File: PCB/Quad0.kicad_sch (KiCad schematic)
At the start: 0 parts

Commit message: implemented basic rp2350 devboard schematics
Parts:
- added C1, C2: 10uF, symbol Device:C_Small
- added C10, C11, C12, C13, C14, C15, C16, C17, C7, C8, C9: 0.1uF, symbol Device:C_Small
- added C18, C19: 15pF, symbol Device:C_Small
- added C3, C4, C5: 4.7uF, symbol Device:C_Small
- added C6: 10u, symbol Device:C_Small
- added J1: DEBUG_CONN_PAD, symbol Connector_Generic:Conn_01x05
- added L1: 3.3u, symbol Device:L_Small
- added Q1: Si2302CDS-T1-GE3, easyeda2kicad:SOT-23_L2.9-W1.3-P1.90-LS2.4-BR, symbol easyeda2kicad:Si2302CDS-T1-GE3
- added R1, R2: 5.1k, symbol Device:R_Small
- added R10, R6, R8, R9: 1k, symbol Device:R_Small
- added R3: 33, symbol Device:R_Small
- added R4, R5: 27, symbol Device:R_Small
- added R7: 10k, symbol Device:R_Small
- added SW1: RUN_BTN, easyeda2kicad:SW-SMD_L3.9-W3.0-P4.45, symbol easyeda2kicad:TS-1088-AR02016
- added SW2: BOOTSEL_BTN, easyeda2kicad:SW-SMD_L3.9-W3.0-P4.45, symbol easyeda2kicad:TS-1088-AR02016
- added U1: RP2350A_C42411118, easyeda2kicad:QFN-60_L7.0-W7.0-P0.40-TL-EP3.4, symbol easyeda2kicad:RP2350A_C42411118
- added U2: AP7361C-33E-13, easyeda2kicad:SOT-223_L6.5-W3.5-P2.30-LS7.0-BR, symbol easyeda2kicad:AP7361C-33E-13
- added U3: W25Q128JVSIQTR, easyeda2kicad:SOIC-8_L5.3-W5.3-P1.27-LS8.0-BL, symbol easyeda2kicad:W25Q128JVSIQTR
- added U4: ABM8-272-T3_C20625731, easyeda2kicad:CRYSTAL-SMD_4P-L3.2-W2.5-BL, symbol easyeda2kicad:ABM8-272-T3_C20625731
- added USB1: TYPE-C 16PIN 2MD, easyeda2kicad:USB-C-SMD_TYPE-C-16PIN-2MD-073, symbol easyeda2kicad:TYPE-C16PIN2MD
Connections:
- new net: R8.1, SW2.2
- new net: C19.2, R10.2, U4.3
- new net: R5.2, U1.51 (USB_DM)
- new net: R6.1, SW1.2
- new net: R2.1, USB1.A5 (CC1)
- new net: R1.1, USB1.B5 (CC2)
- new net: R4.1, U1.52 (USB_DP)
- new net: C3.1, R3.2, U1.46 (VREG_AVDD)
- new net: L1.2, U1.48 (VREG_LX)
- new net +1V1: C15.2, C16.2, C17.2, C5.2, L1.1, U1.23 (DVDD), U1.39 (DVDD), U1.50 (VREG_FB), U1.6 (DVDD)
- new net +3.3V: C10.2, C11.2, C12.2, C13.2, C14.2, C2.1, C4.2, C6.1, C7.1, C8.2, C9.2, R3.1, R7.1, U1.1 (IOVDD), U1.11 (IOVDD), U1.20 (IOVDD), U1.30 (IOVDD), U1.38 (IOVDD), U1.44 (ADC_AVDD), U1.45 (IOVDD), U1.49 (VREG_VIN), U1.53 (USB_OTP_VDD), U1.54 (QSPI_IOVDD), U2.3 (OUT), U3.8 (VCC)
- new net GND: C1.2, C10.1, C11.1, C12.1, C13.1, C14.1, C15.1, C16.1, C17.1, C18.1, C19.1, C2.2, C3.2, C4.1, C5.1, C6.2, C7.2, C8.1, C9.1, J1.1 (Pin_1), J1.2 (Pin_2), J1.4 (Pin_4), R1.2, R2.2, R6.2, R8.2, U1.47 (VREG_PGND), U1.61 (GND), U2.2 (GND), U2.4 (GND), U3.4 (GND), U4.2 (GND), U4.4 (GND), USB1.13 (EH), USB1.14 (EH), USB1.A1B12 (GND), USB1.B1A12 (GND)
- new net GPIO0: U1.2 (GPIO0)
- new net GPIO1: U1.3 (GPIO1)
- new net GPIO10: U1.14 (GPIO10)
- new net GPIO11: U1.15 (GPIO11)
- new net GPIO12: U1.16 (GPIO12)
- new net GPIO13: U1.17 (GPIO13)
- new net GPIO14: U1.18 (GPIO14)
- new net GPIO15: U1.19 (GPIO15)
- new net GPIO16: U1.27 (GPIO16)
- new net GPIO17: U1.28 (GPIO17)
- new net GPIO18: U1.29 (GPIO18)
- new net GPIO19: U1.31 (GPIO19)
- new net GPIO2: U1.4 (GPIO2)
- new net GPIO20: U1.32 (GPIO20)
- new net GPIO21: U1.33 (GPIO21)
- new net GPIO22: U1.34 (GPIO22)
- new net GPIO23: U1.35 (GPIO23)
- new net GPIO24: U1.36 (GPIO24)
- new net GPIO25: U1.37 (GPIO25)
- new net GPIO26: U1.40 (GPIO26_ADC0)
- new net GPIO27: U1.41 (GPIO27_ADC1)
- new net GPIO28: U1.42 (GPIO28_ADC2)
- new net GPIO29: U1.43 (GPIO29_ADC3)
- new net GPIO3: U1.5 (GPIO3)
- new net GPIO4: U1.7 (GPIO4)
- new net GPIO5: U1.8 (GPIO5)
- new net GPIO6: U1.9 (GPIO6)
- new net GPIO7: U1.10 (GPIO7)
- new net GPIO8: U1.12 (GPIO8)
- new net GPIO9: U1.13 (GPIO9)
- new net MCU_RUN: SW1.1, U1.26 (RUN)
- new net MCU_SWCLK: J1.5 (Pin_5), U1.24 (SWCLK)
- new net MCU_SWDIO: J1.3 (Pin_3), U1.25 (SWDIO)
- new net MCU_XIN: C18.2, U1.21 (XIN), U4.1
- new net MCU_XOUT: R10.1
- new net QSPI_SCLK: U1.56 (QSPI_SCLK), U3.6 (CLK)
- new net QSPI_SD0: U1.57 (QSPI_SD0), U3.2 (DO)
- new net QSPI_SD1: U1.59 (QSPI_SD1), U3.5 (DI)
- new net QSPI_SD2: U1.58 (QSPI_SD2), U3.3 (IO2)
- new net QSPI_SD3: U1.55 (QSPI_SD3), U3.7 (IO3)
- new net QSPI_SS: R7.2, R9.2, U1.60 (QSPI_SS), U3.1 (~{CS})
- new net USB_D+: R4.2, USB1.A6 (Dp1), USB1.B6 (Dp2)
- new net USB_D-: R5.1, USB1.A7 (Dn1), USB1.B7 (Dn2)
- new net VBUS: C1.1, U2.1 (IN), USB1.A4B9 (VBUS), USB1.B4A9 (VBUS)
- new net ~{USB_BOOT}: R9.1, SW2.1
- no-connect marks 0 -> 2
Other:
- note added: "12MHz Crystal"
- note added: "3V3 Regulator"
- note added: "BOOTSEL BTN"
- note added: "FLASH"
- note added: "GPIO Tracker"
- note added: "Microcontroller RP2350"
- note added: "RUN BTN"
- note added: "USB-C Receptacle"
- note added: "marked DNP by official min devboard schematics by RPi"

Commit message: follow the cap naming convention
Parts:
- C6: value 10u -> 10uF
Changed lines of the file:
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@@
 			)
 		)
-		(property "Value" "10u"
+		(property "Value" "10uF"
 			(at 143.51 44.4562 0)
 			(effects

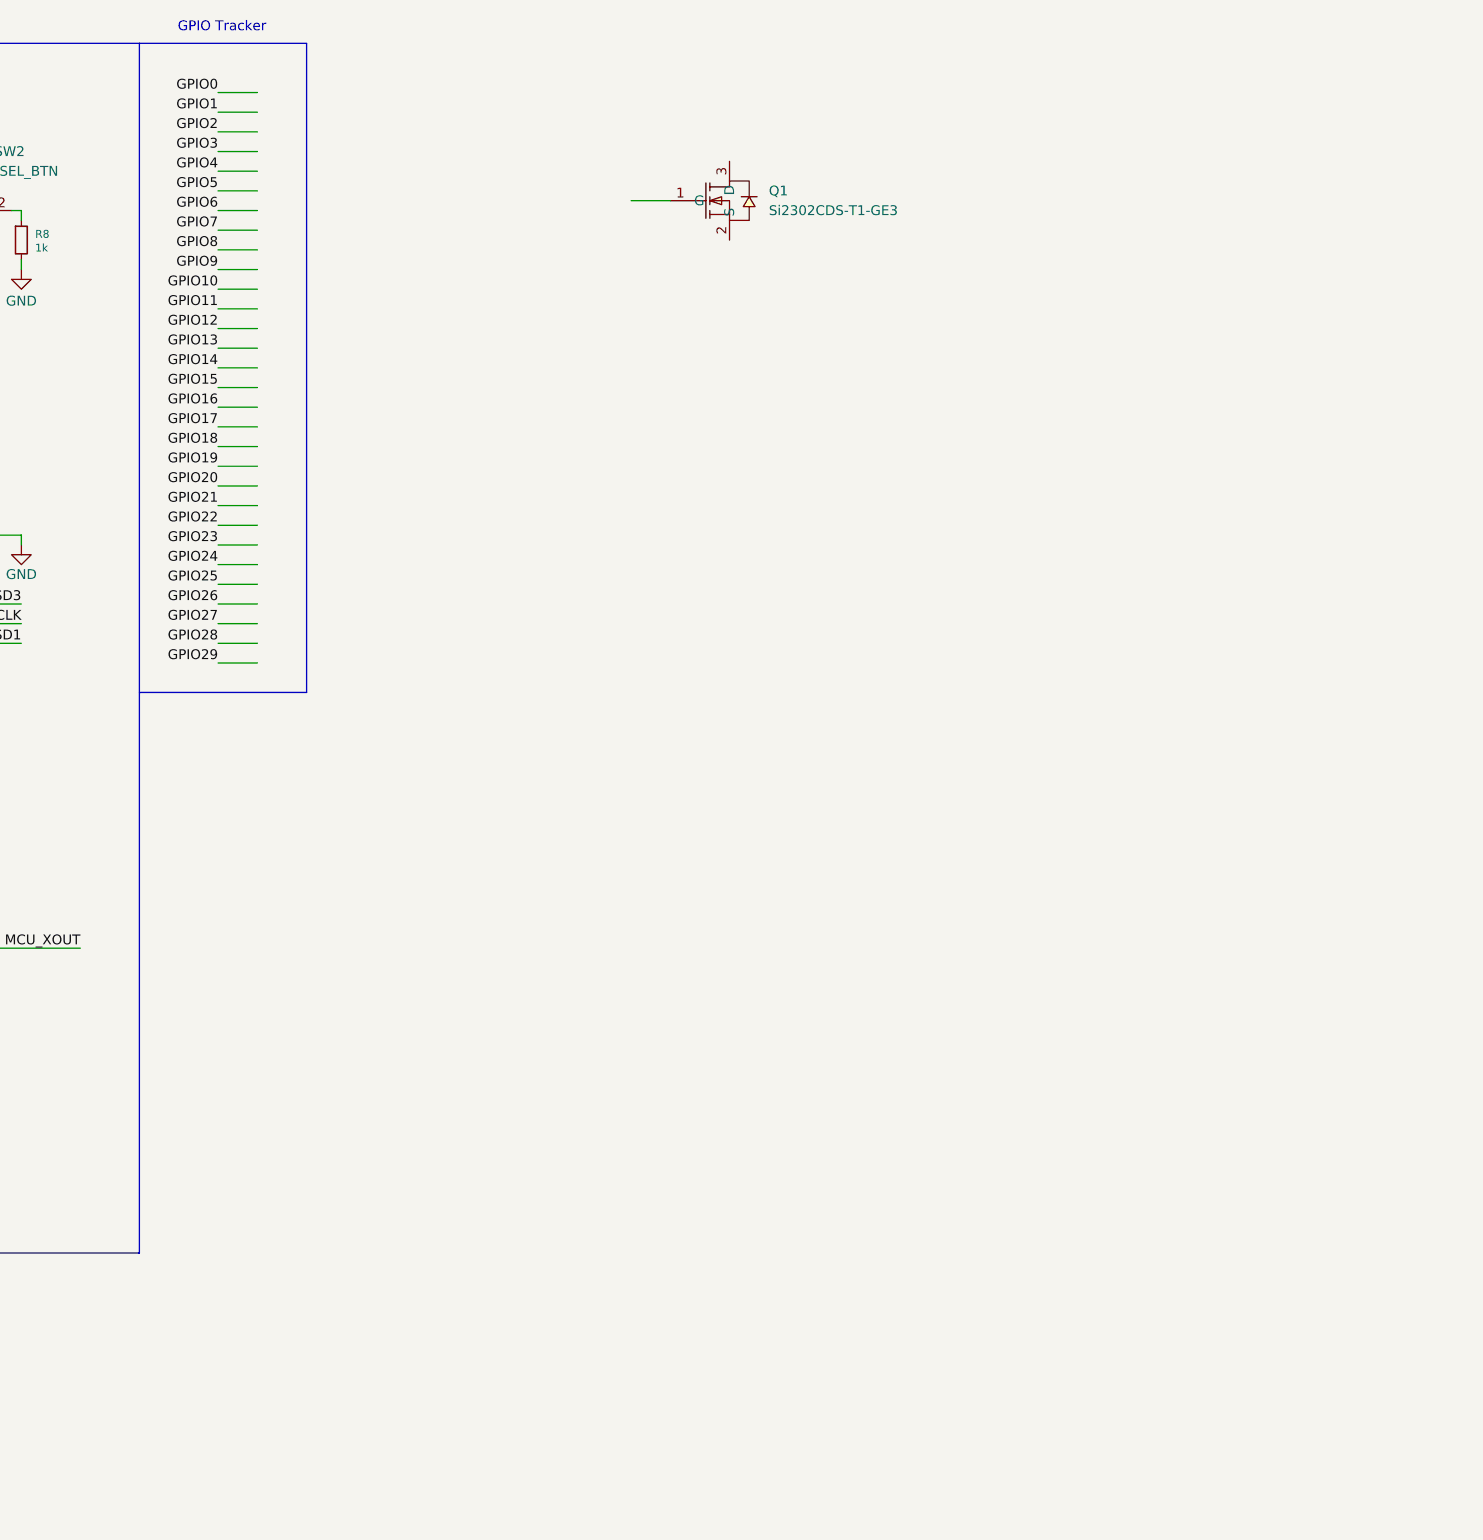
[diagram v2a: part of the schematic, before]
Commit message: added brushed motor drivers
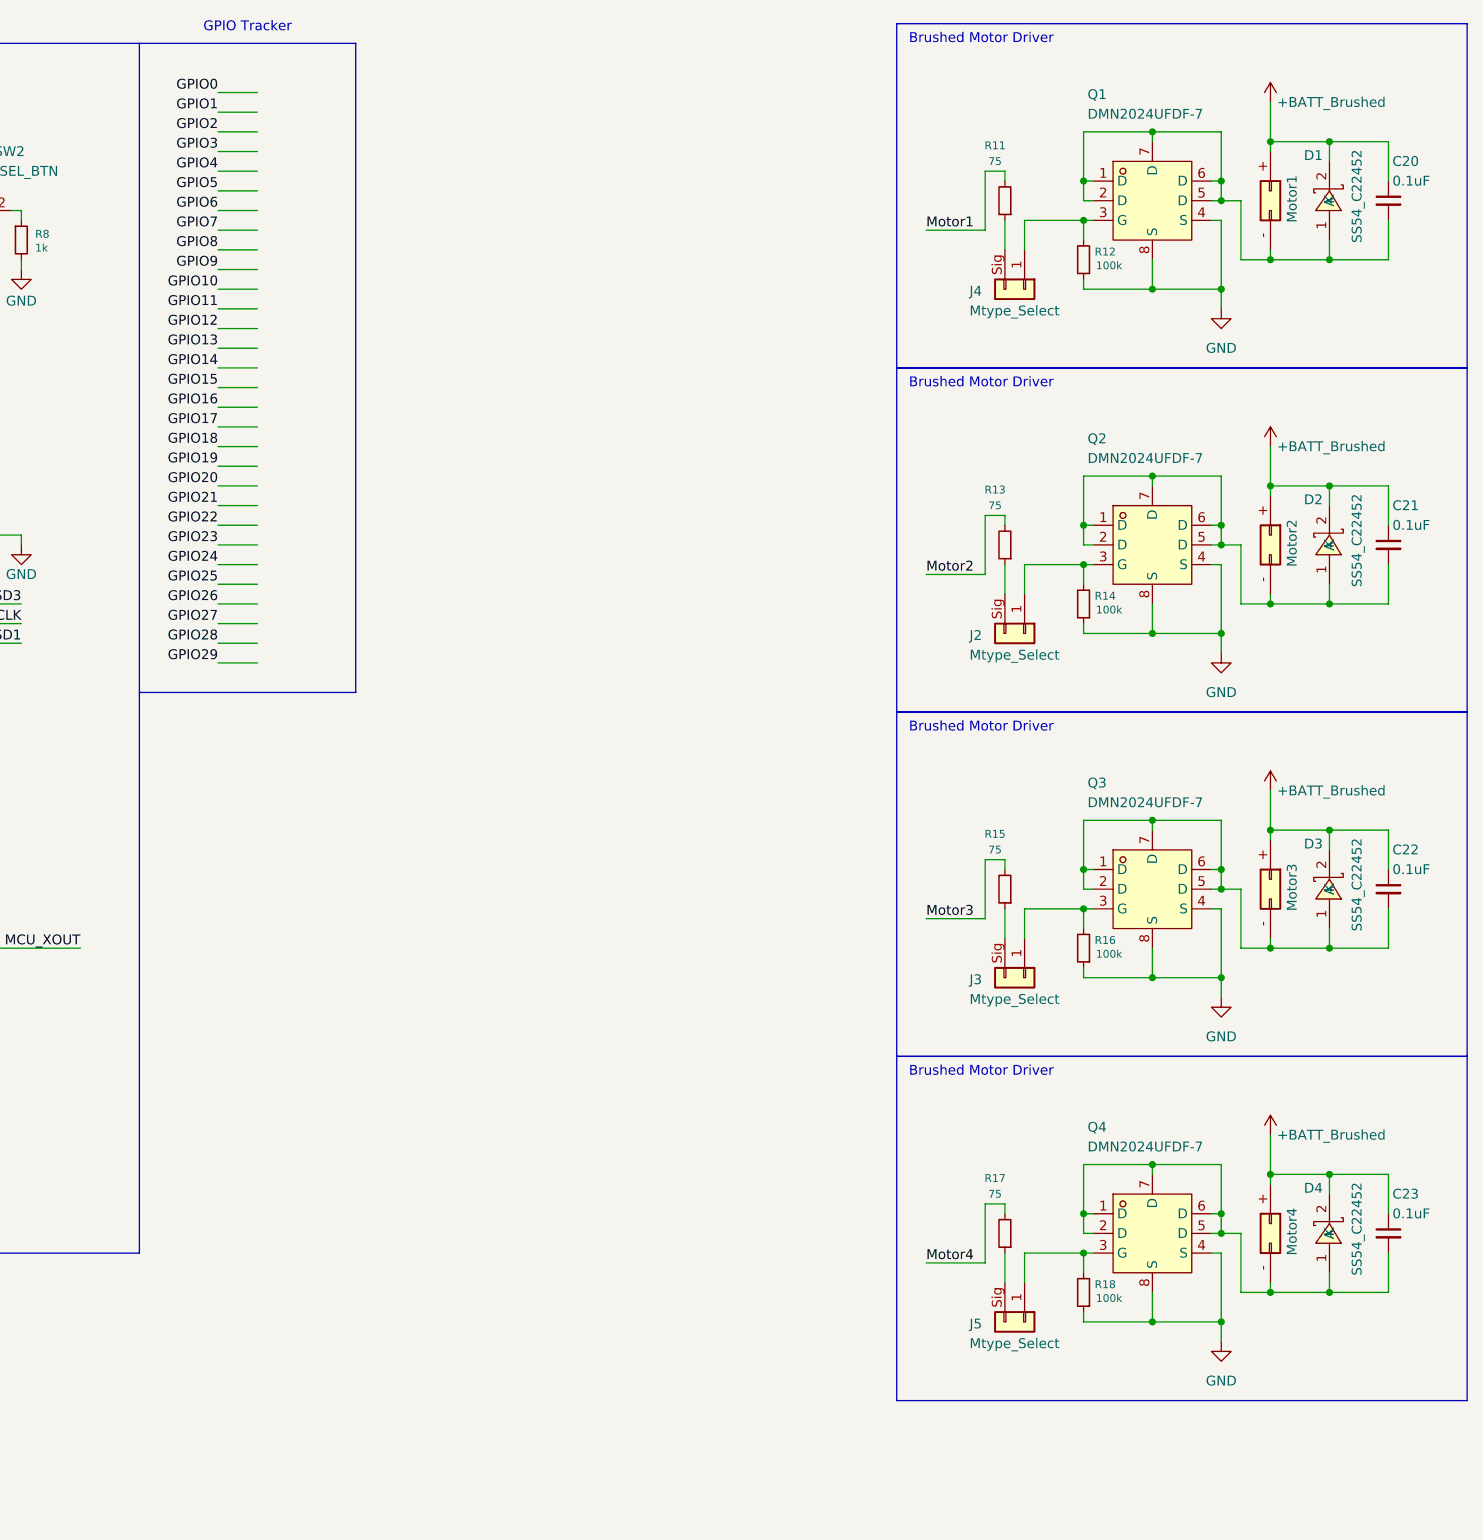
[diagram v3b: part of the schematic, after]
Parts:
- removed Q1: Si2302CDS-T1-GE3, easyeda2kicad:SOT-23_L2.9-W1.3-P1.90-LS2.4-BR, symbol easyeda2kicad:Si2302CDS-T1-GE3
- added C20, C21, C22, C23: 0.1uF, symbol Device:C_Small
- added D1, D2, D3, D4: SS54_C22452, easyeda2kicad:SMA_L4.4-W2.8-LS5.4-R-RD, symbol easyeda2kicad:SS54_C22452
- added J2, J3, J4, J5: Mtype_Select, symbol Connector_Generic:Conn_01x02
- added Motor1, Motor2, Motor3, Motor4: motor, symbol Connector_Generic:Conn_02x01
- added Q1, Q2, Q3, Q4: DMN2024UFDF-7, easyeda2kicad:DFN2020MD-6_L2.0-W2.0-P0.65-BL, symbol easyeda2kicad:DMN2024UFDF-7
- added R11, R13, R15, R17: 75, symbol Device:R_Small
- added R12, R14, R16, R18: 100k, symbol Device:R_Small
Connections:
- net GND: now also Q1.4 (S), Q1.8 (S), Q2.4 (S), Q2.8 (S), Q3.4 (S), Q3.8 (S), Q4.4 (S), Q4.8 (S), R12.1, R14.1, R16.1, R18.1
- new net: J4.Sig (Pin_2), R11.1
- new net: C23.2, D4.1 (A), Motor4.- (Pin_2), Q4.1 (D), Q4.2 (D), Q4.5 (D), Q4.6 (D), Q4.7 (D)
- new net: J2.Sig (Pin_2), R13.1
- new net: J4.1 (Pin_1), Q1.3 (G), R12.2
- new net: J3.1 (Pin_1), Q3.3 (G), R16.2
- new net: J5.1 (Pin_1), Q4.3 (G), R18.2
- new net: J2.1 (Pin_1), Q2.3 (G), R14.2
- new net: C22.2, D3.1 (A), Motor3.- (Pin_2), Q3.1 (D), Q3.2 (D), Q3.5 (D), Q3.6 (D), Q3.7 (D)
- new net: C20.2, D1.1 (A), Motor1.- (Pin_2), Q1.1 (D), Q1.2 (D), Q1.5 (D), Q1.6 (D), Q1.7 (D)
- new net: J3.Sig (Pin_2), R15.1
- new net: C21.2, D2.1 (A), Motor2.- (Pin_2), Q2.1 (D), Q2.2 (D), Q2.5 (D), Q2.6 (D), Q2.7 (D)
- new net: J5.Sig (Pin_2), R17.1
- new net +BATT_Brushed: C20.1, C21.1, C22.1, C23.1, D1.2 (K), D2.2 (K), D3.2 (K), D4.2 (K), Motor1.+ (Pin_1), Motor2.+ (Pin_1), Motor3.+ (Pin_1), Motor4.+ (Pin_1)
- new net Motor1: R11.2
- new net Motor2: R13.2
- new net Motor3: R15.2
- new net Motor4: R17.2
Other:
- note added: "Brushed Motor Driver"

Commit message: added imu schematics, usb reverse current protection and wired everything to the appropriate gpio pins
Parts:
- added C24, C25, C26, C27: 0.1uF, symbol Device:C_Small
- added H1, H2, H3, H4: MountingHole, symbol Mechanical:MountingHole
- added J6: 1N5819, symbol Connector_Generic:Conn_01x02
- added J7: Power_Pad, symbol Connector_Generic:Conn_01x02
- added R19, R20: 4.7k, symbol Device:R_Small
- added U5: ICM-42688-P, easyeda2kicad:LGA-14_L3.0-W2.5-P0.50-BL, symbol easyeda2kicad:ICM-42688-P
- added U6: DPS368XTSA1, easyeda2kicad:LGA-8_L2.5-W2.0-P0.65-TR_DPS368, symbol easyeda2kicad:DPS368XTSA1
- J1, J2, J3, J4, J5, Motor1, Motor2, Motor3, Motor4, R7: now left out of the parts list
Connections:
- net Motor1 is gone; now on net GPIO11: R11.2
- net Motor2 is gone; now on net GPIO12: R13.2
- net Motor3 is gone; now on net GPIO13: R15.2
- net Motor4 is gone; now on net GPIO14: R17.2
- net +3.3V: now also C24.2, C25.2, C26.1, C27.1, R19.2, R20.1, U5.5 (VDDIO), U5.8 (VDD), U6.6 (VDDIO), U6.8 (VDD)
- net +BATT_Brushed: now also C1.1, U2.1 (IN), USB1.A4B9 (VBUS), J6.K (Pin_2), J7.PWR (Pin_1)
- net GND: now also C24.1, C25.1, C26.2, C27.2, J7.GND (Pin_2), U5.6 (GND), U5.7 (RESV), U6.1 (GND), U6.7 (GND)
- net GPIO2: now also U5.13 (SCK)
- net GPIO3: now also U5.14 (SDA)
- net GPIO4: now also U5.1 (SDO)
- net GPIO5: now also U5.12 (SENB)
- net GPIO6: now also U5.4 (INT1)
- net GPIO7: now also U5.9 (INT2)
- net GPIO0 renamed BAR_SDA
- net BAR_SDA: now also R19.1, U6.3 (SDI)
- net GPIO1 renamed BAR_SCL
- net BAR_SCL: now also R20.2, U6.4 (SCK)
- net GPIO8 renamed BAR_INT
- net BAR_INT: now also U6.5 (SDO)
- removed net VBUS: C1.1, U2.1 (IN), USB1.A4B9 (VBUS), USB1.B4A9 (VBUS)
- new net USB_RAW_VBUS: J6.A (Pin_1), USB1.B4A9 (VBUS)
- no-connect marks 2 -> 24
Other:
- note added: "Accelerometer & Gyroscope"
- note added: "Barometer"
- note added: "Can be shorted if necessary, Make sure not to connect battery and USB at the same time."
- note added: "PCB Mounting Holes"
- note added: "Power Pad"
- note added: "Through-Hole so it's easier to replace"
- note added: "USB Back-Current Protection"
- note added: "[Rating: 2.2V ~ 6.0V] - ESC BEC (5V 2A) - 1s LiPo (3.0-4.2V) - USB (5V ~1A)"
- moved on the sheet: C1, C2, C20, C21, C22, C23, D1, D2, D3, D4, J2, J3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

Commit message: added barometer
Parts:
- added C28, C29: 0.1uF, symbol Device:C_Small
- added R21: 100k, symbol Device:R_Small
- added U7: BMM150, easyeda2kicad:WLCSP-12_L1.6-W1.6_BMM150, symbol easyeda2kicad:BMM150
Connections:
- net +3.3V: now also C28.1, C29.2, U7.A1 (PS), U7.B2 (VDDIO), U7.E5 (VDD)
- net BAR_INT: now also R21.1
- net BAR_SCL: now also U7.A3 (SCK)
- net BAR_SDA: now also U7.B4 (SDI)
- net GND: now also C28.2, C29.1, R21.2, U7.A5 (CSB), U7.C1 (SDO), U7.C5 (GND), U7.E1 (GND), U7.E3 (GND)
- net GPIO10: now also U7.D4 (DRY)
- net GPIO9: now also U7.D2 (INT)
- no-connect marks 24 -> 22
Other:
- note added: "Brushed Motor Drivers"
- note added: "CSB = SDO = GND >> I2C Addr = 0x10"
- note added: "I2C ADDRESS 0x76 -> (SDO == GND)"
- note added: "Inertial Measurement Unit"
- note added: "Magnetometer"
- note added: "Microcontroller Unit"
- moved on the sheet: C1, C10, C11, C12, C13, C14, C15, C16, C17, C18, C19, C2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

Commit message: added wifi transceiver
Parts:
- added U8: ESP-01, easyeda2kicad:WIFIM-TH_8P-L24.7-W14.4-P2.54, symbol easyeda2kicad:ESP-01
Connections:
- net +3.3V: now also U8.6 (EN), U8.8 (VCC)
- net GND: now also U8.1 (GND)
- net GPIO16: now also U8.4 (RXD)
- net GPIO17: now also U8.5 (TXD)
- no-connect marks 22 -> 23
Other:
- note added: "DNP as hand-soldered & upto user"
- note added: "For brushed mode: ESP01 WiFi module For brushless mode: RF Receiver"
- note added: "Signal: WIFI_RX Power: Pin 8 or 6 GND: Pin 1"
- note added: "Since the footprint is 2x4 2.54mm headers, and the RF receiver module that I have is also connected using jumper wires, the pinout for the RF receiver is:"
- note added: "Status / Power Indication"
- note added: "WiFi Transceiver / RF receiver"
- moved on the sheet: C20, C21, C22, C23, C24, C25, C26, C27, C28, C29, D1, D2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

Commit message: added leds, fuel gauge schematic
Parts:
- added C30, C31: 0.1uF, symbol Device:C_Small
- added C32: 10uF, symbol Device:C_Small
- added LED1, LED2: 17-21SUYC/TR8, easyeda2kicad:LED0805-R-RD, symbol easyeda2kicad:17-21SUYC_TR8
- added R22, R23: 120, symbol Device:R_Small
- added R24, R25: 10k, symbol Device:R_Small
- added R26: 15k, symbol Device:R_Small
- added U9: AP22818BKWT-7, easyeda2kicad:TSOT-23-5_L2.9-W1.6-P0.95-LS2.8-BL, symbol easyeda2kicad:AP22818BKWT-7
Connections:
- net +3.3V: now also LED1.1 (+)
- net +BATT_Brushed: now also C30.1, R24.1, U9.4 (IN)
- net GND: now also C30.2, C31.1, C32.1, R22.2, R23.2, R26.2, U9.2 (GND)
- net GPIO15: now also LED2.1 (+)
- net GPIO25 renamed BAT_SENSE_EN
- net BAT_SENSE_EN: now also U9.3 (EN)
- net GPIO26 renamed BAT_SENSE_VD
- net BAT_SENSE_VD: now also R25.2, R26.1
- new net: R24.2, U9.1 (FLG)
- new net: LED1.2 (-), R22.1
- new net: LED2.2 (-), R23.1
- new net BAT_SENSE_RAW: C31.2, C32.2, R25.1, U9.5 (OUT)
- no-connect marks 23 -> 20
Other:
- note added: "Voltage Divider: 0-5.5V -> 0-3.3V"
- note added: "[Rating: 2.2V ~ 5.5V] - ESC BEC (5V 2A) - 1s LiPo (3.0-4.2V) - USB (5V ~1A)"
- note removed: "[Rating: 2.2V ~ 6.0V] - ESC BEC (5V 2A) - 1s LiPo (3.0-4.2V) - USB (5V ~1A)"
